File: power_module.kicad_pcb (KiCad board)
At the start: 4 copper layers, 95 x 76.9 mm, 71 parts, among them J1 USB_C_PD, J2 OUTPUT, J3 I2C_BREAKOUT, Q1 DUAL_N_FET, Q2 DUAL_N_FET, Q3 DUAL_N_FET, Q4 DUAL_N_FET, SW1 ON_OFF, U1 BQ7692003, U2 CH224K, U3 BQ24650, U4 LM5176PWPR

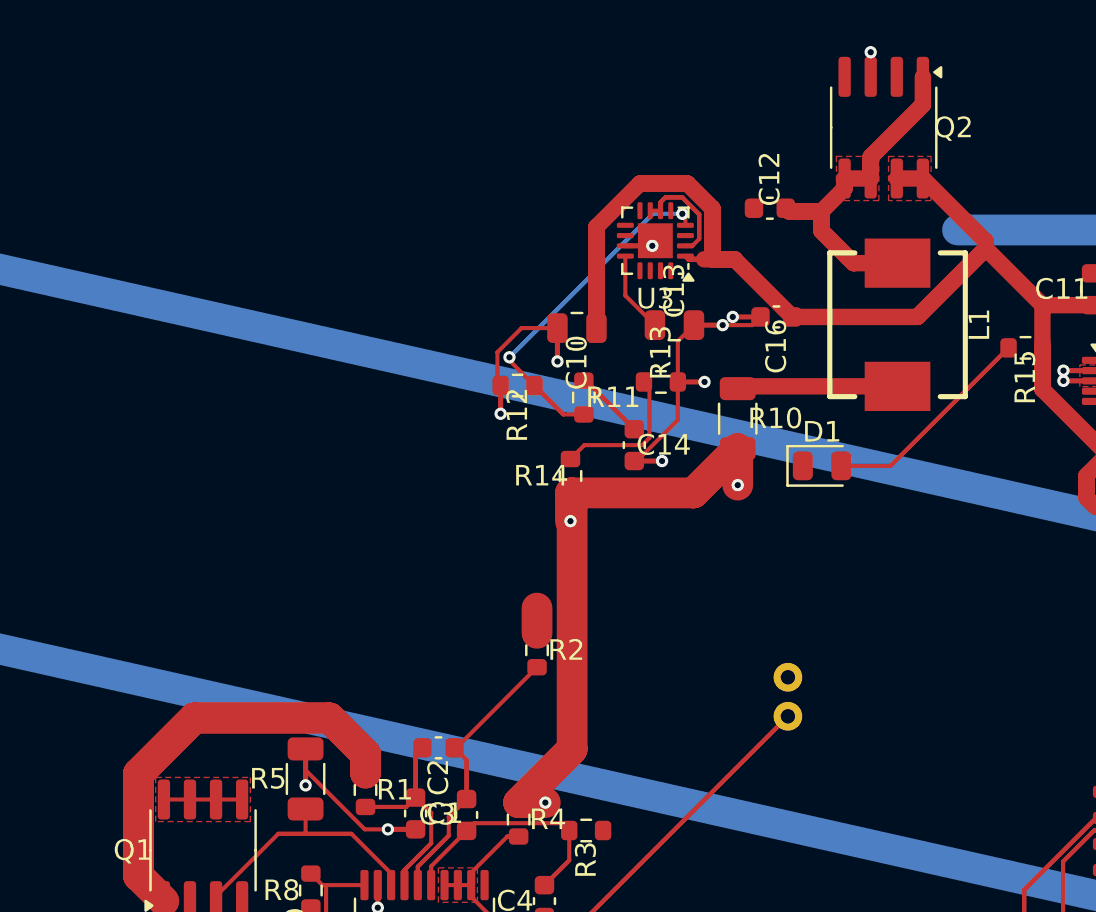
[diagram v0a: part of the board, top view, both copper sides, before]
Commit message: close BAT- east-end unconnect (#210)
Bridges F.Cu BMS island to existing B.Cu east trunk via top-of-board
corridor: F.Cu vertical at x=20.12 (38.93->8) + via + B.Cu horizontal
at y=8 (20.12->60) + B.Cu short south to existing trunk end (60,12.45).

26 -> 25 unconnects; refill_zones cleared new inner-plane via clearance
flags. DRC: 149 -> 147 violations.

Co-Authored-By: Claude Opus 4.7 <noreply@anthropic.com>
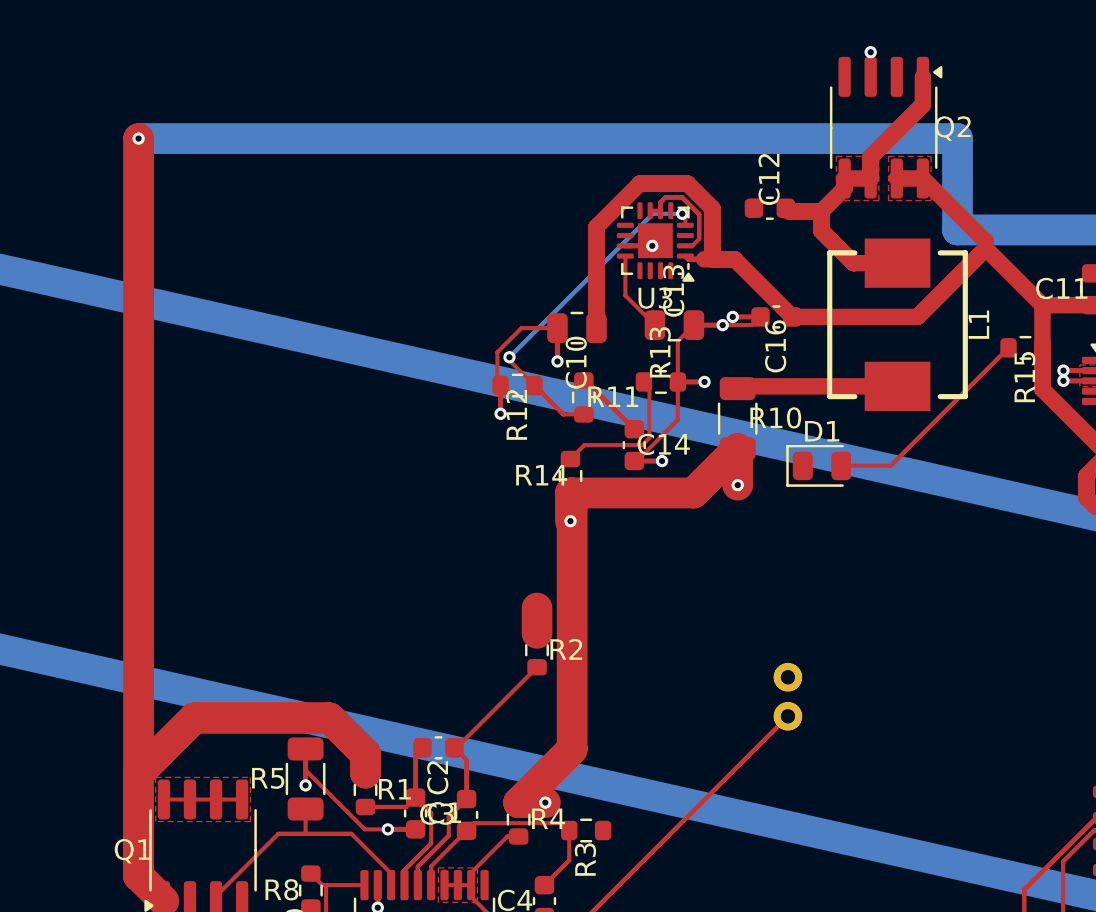
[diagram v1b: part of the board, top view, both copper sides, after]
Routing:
- net BAT-: track 66.5 -> 141.8 mm, vias 0 -> 1
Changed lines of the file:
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@@
+	)
+	(segment
+		(start 20.12 38.93)
+		(end 20.12 8)
+		(width 1.5)
+		(layer "F.Cu")
+		(net 31)
 	)
 	(segment
@@
 		(net 31)
 	)
+	(via
+		(at 20.12 8)
+		(size 0.6)
+		(drill 0.3)
+		(layers "F.Cu" "B.Cu")
+		(net 31)
+	)
+	(segment
+		(start 60 8)
+		(end 60 12.45)
+		(width 1.5)
+		(layer "B.Cu")
+		(net 31)
+	)
 	(segment
 		(start 87.1544 12.4482)
@@
 		(width 1.5)
 		(layer "B.Cu")
+		(net 31)
+	)
+	(segment
+		(start 20.12 8)
+		(end 60 8)
+		(width 1.5)
+		(layer "B.Cu")

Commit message: add 4 BAT+ via stubs to bridge orphan F.Cu islands to In2.Cu plane (#169)
Vias at (71.62,63.90) C8.1, (70.79,53.48), (36.77,50.08), (72.52,39.81)
— closes 1 BAT+ ratsnest gap. The rest of the BAT+ unconnects need
trace re-routing (C8↔C28 area is congested with U4 BB_* signals;
SW1.2 and U3.9 need pin-escape stubs that conflict with adjacent
nets).

DRC: 147 -> 146 violations; 25 -> 24 unconnects; no new shorts or
dangling traces.

Co-Authored-By: Claude Opus 4.7 <noreply@anthropic.com>
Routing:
- net BAT+: vias 9 -> 13
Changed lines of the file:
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@@
+	)
+	(via
+		(at 71.62 63.9)
+		(size 0.6)
+		(drill 0.3)
+		(layers "F.Cu" "B.Cu")
+		(net 1)
+	)
+	(via
+		(at 36.77 50.08)
+		(size 0.6)
+		(drill 0.3)
+		(layers "F.Cu" "B.Cu")
+		(net 1)
 	)
 	(via
@@
 	)
 	(via
+		(at 70.79 53.48)
+		(size 0.6)
+		(drill 0.3)
+		(layers "F.Cu" "B.Cu")
+		(net 1)
+	)
+	(via
 		(at 33.8067 57.938)
 		(size 0.6)
@@
 		(size 0.6)
 		(drill 0.3)
+		(layers "F.Cu" "B.Cu")
+		(net 1)
+	)
+	(via
+		(at 72.52 39.81)
+		(size 0.6)
+		(drill 0.3)

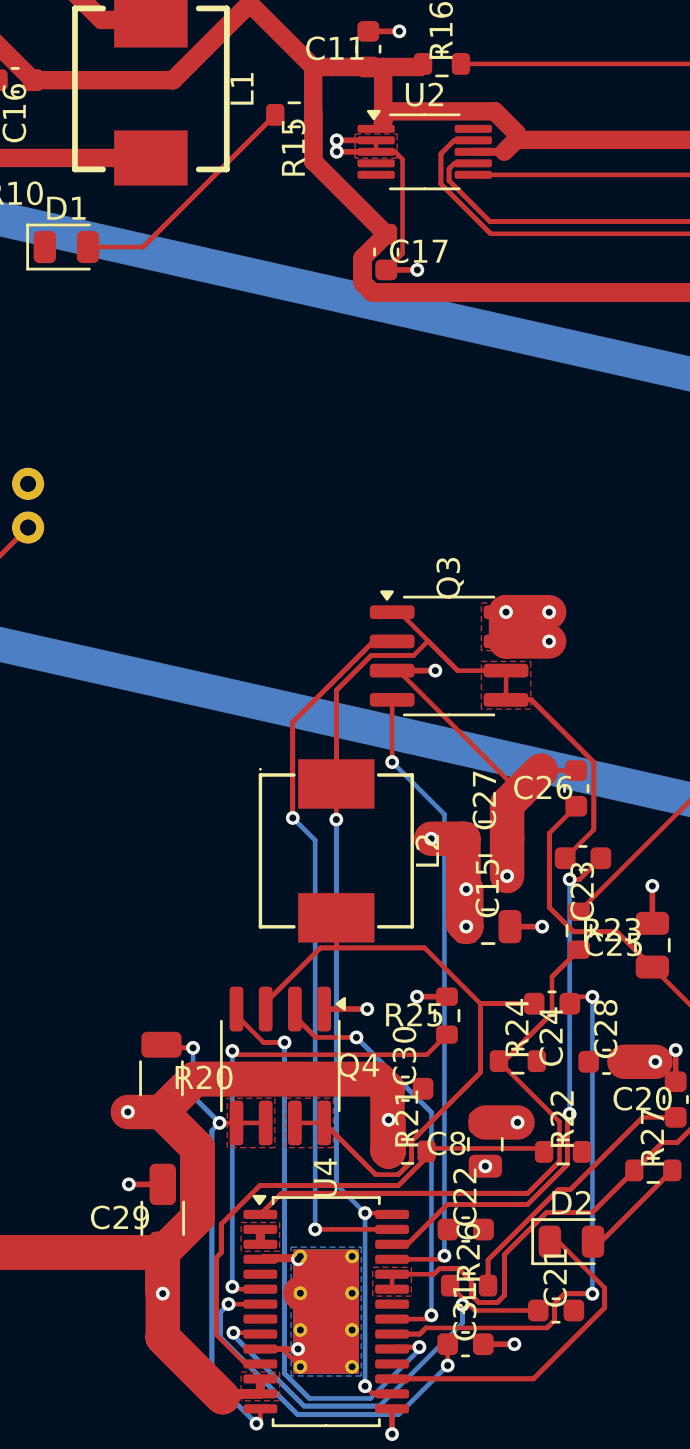
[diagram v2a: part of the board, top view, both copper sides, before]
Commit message: fix U4 GND thermal-pad bond + clean up redundant GND vias (#221)
- Add via at U4 pin 22 (67.564, 69.893) to bond it to the In1.Cu GND
  plane. Pin 22 was a F.Cu-only SMD pad isolated from U4's thermal
  pad island because the F.Cu GND zone had a void around the IC body.
  Closes the U4.22 <-> U4.29 ratsnest gap.
- Delete stacked GND via at (65.158699, 19.7992) — was 0.5mm from
  the (65.158699, 19.2992) via (hole_to_hole error).
- Delete redundant GND via at (63.4765, 67.943) — overlapped U4's
  own thermal-pad PTH via at (63.5765, 67.818) (hole_to_hole error).
- Delete the now-orphan GND L-bend stubs that were leading to the
  removed vias.

DRC: 145 -> 142 violations; 36 -> 35 errors; all 3 hole_to_hole
errors resolved; 24 -> 23 unconnects.

Co-Authored-By: Claude Opus 4.7 <noreply@anthropic.com>
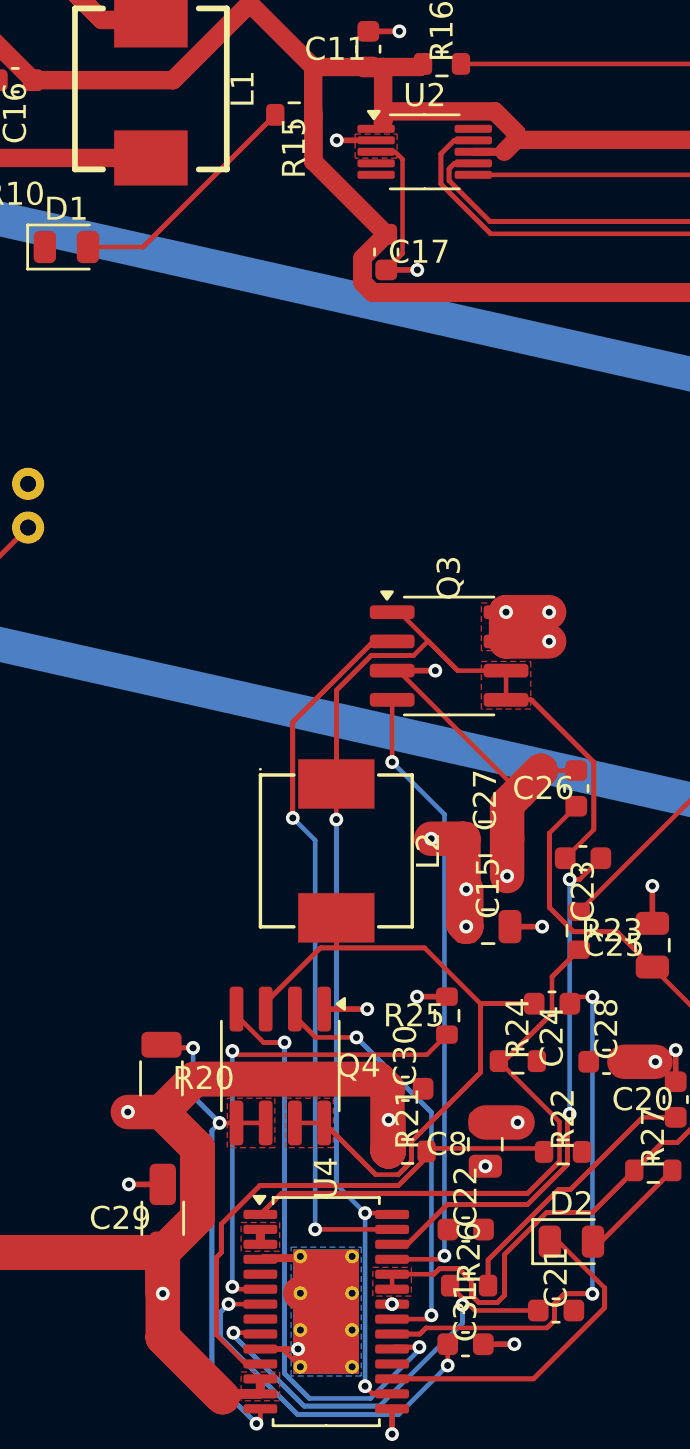
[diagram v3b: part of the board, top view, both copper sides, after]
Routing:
- net GND: track 108.9 -> 105.8 mm, vias 35 -> 34
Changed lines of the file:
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@@
-	)
-	(segment
-		(start 66.8712 19.7992)
-		(end 67.6982 19.7992)
-		(width 0.2)
-		(layer "F.Cu")
-		(net 5)
 	)
 	(segment
@@
 	)
 	(segment
-		(start 66.8712 19.7992)
-		(end 65.158699 19.7992)
-		(width 0.25)
-		(layer "F.Cu")
-		(net 5)
-	)
-	(segment
 		(start 61.964 67.818)
 		(end 61.839 67.943)
@@
 	)
 	(segment
-		(start 66.8712 19.2992)
-		(end 66.8712 19.7992)
-		(width 0.2)
-		(layer "F.Cu")
-		(net 5)
-	)
-	(segment
 		(start 47.1648 17.0835)
 		(end 46.3817 17.8666)
@@
 	)
 	(via
-		(at 63.4765 67.943)
-		(size 0.6)
-		(drill 0.3)
-		(layers "F.Cu" "B.Cu")
-		(net 5)
-	)
-	(via
 		(at 49.0558 16.684)
 		(size 0.6)
@@
 	)
 	(via
+		(at 67.564 69.893)
+		(size 0.6)
+		(drill 0.3)
+		(layers "F.Cu" "B.Cu")
+		(net 5)
+	)
+	(via
 		(at 31.7687 45.454)
 		(size 0.6)
@@
 		(size 0.6)
 		(drill 0.3)
-		(layers "F.Cu" "B.Cu")
-		(net 5)
-	)
-	(via
-		(at 65.158699 19.7992)
-		(size 0.6)
-		(drill 0.3)
